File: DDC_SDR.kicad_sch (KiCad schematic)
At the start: 101 parts, among them J13 AWG_OUT, J14 DUT, J16 S21_OUT, J3 Filter, J4 Filter, J6 PMOD, Q10 2N7002, Q3 2N7002, U15 TPH2501-TR, U2 MS9280, U25 TPH2501-TR, U26 74LVC1G3157GW, U27 74LVC1G3157GW, U3 MS9708, U7 ICE40UP5K-SG48ITR

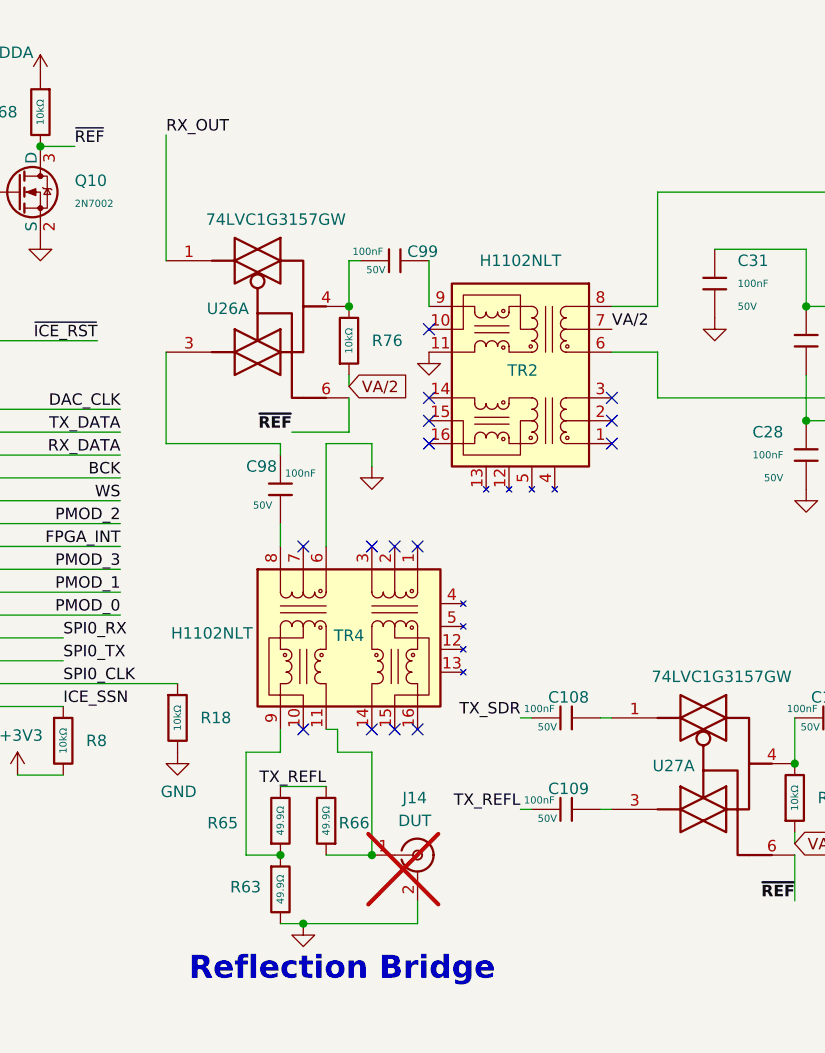
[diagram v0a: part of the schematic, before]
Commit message: Added provision for switch leakage current.
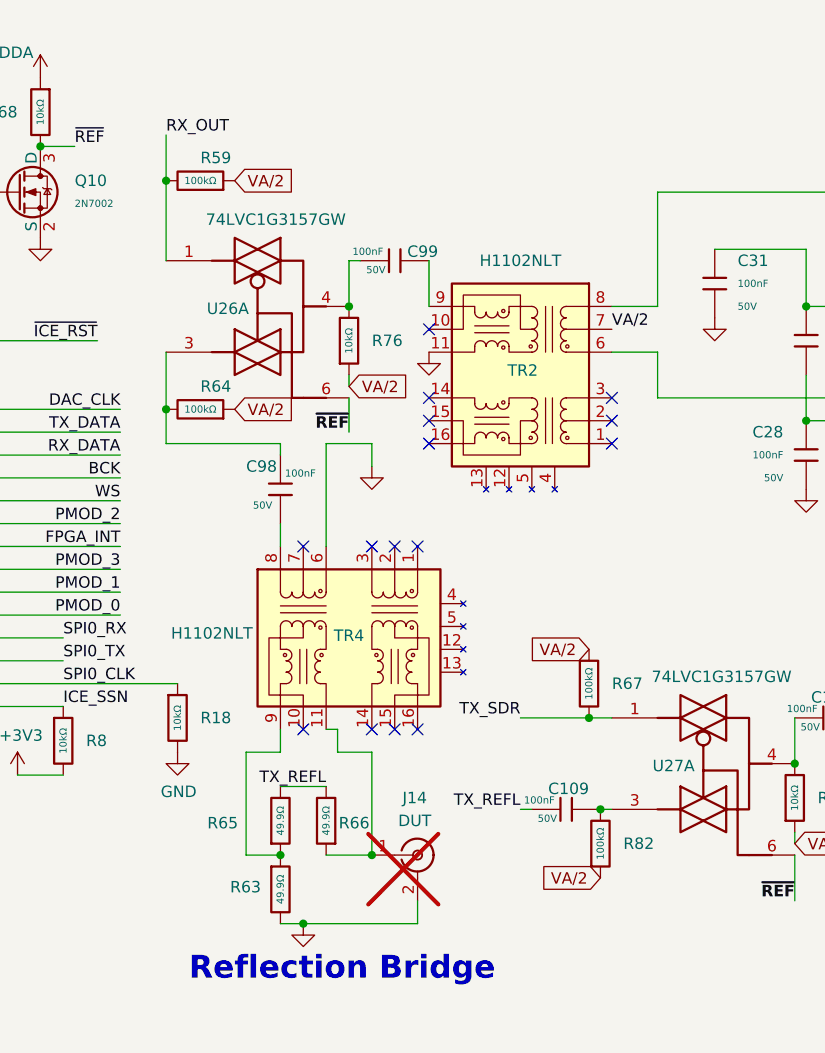
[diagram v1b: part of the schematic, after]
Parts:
- removed C108: 100nF, PCM_JLCPCB:C_0402, symbol PCM_JLCPCB-Capacitors:0402,100nF,(2)
- added R59, R64, R67, R82: 100kΩ, PCM_JLCPCB:R_0402, symbol PCM_JLCPCB-Resistors:0402,100kΩ
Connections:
- net RX_OUT: now also R59.2
- net TX_SDR: now also U27.1, R67.2
- net VA/2: now also R59.1, R64.1, R67.1, R82.1
- net at C98.1, U26.3: now also R64.2
- net at C109.2, U27.3: now also R82.2

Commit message: Minor tweaks...
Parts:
- added R83, R84: 22Ω, PCM_JLCPCB:R_0402, symbol PCM_JLCPCB-Resistors:0402,22Ω
- U7: Price $0.09 -> $8.49
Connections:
- net PMOD_3: now also JP51.2 (B), R30.2; no longer J6.4 (Pin_4), JP51.1 (A)
- net SPI0_RX: now also R83.1; no longer A2.6 (GPIO4)
- net SPI0_TX: now also R84.1; no longer A2.10 (GPIO7)
- new net: A2.10 (GPIO7), R84.2
- new net: A2.6 (GPIO4), R83.2
- new net: J6.4 (Pin_4), JP51.1 (A)
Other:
- note added: "Put the GBIN_PMOD_3 right by the PMOD connector. Then daisy-chain route this trace."
- note added: "WS (LRCK) pin must be BCK pin +1"
- note removed: "LRCK pin must be BCK pin +1"

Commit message: Starting to place components
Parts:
- A2: footprint Module:RaspberryPi_Pico_W_SMD_HandSolder -> Module:RaspberryPi_Pico_Common_THT
- C15: footprint PCM_JLCPCB:C_0805 -> PCM_JLCPCB:C_0603; symbol PCM_JLCPCB-Capacitors:0805,1uF -> PCM_JLCPCB-Capacitors:0603,1uF; LCSC C28323 -> C15849; Part CL21B105KBFNNNE -> CL10A105KB8NNNC; Price 0.012USD -> 0.008USD; Stock 4334256 -> 11535980; Temperature Coefficient X7R -> X5R
- C23, C30, C34, C93: footprint PCM_JLCPCB:C_0805 -> PCM_JLCPCB:C_0402; symbol PCM_JLCPCB-Capacitors:0805,100nF -> PCM_JLCPCB-Capacitors:0402,100nF,(2); LCSC C28233 -> C307331; Manufacturer (none) -> Samsung Electro-Mechanics; Part CL21B104KCFNNNE -> CL05B104KB54PNC; Price 0.009USD -> 0.008USD; Stock 1168020 -> 8389599; Voltage Rated 100V -> 50V
- C44: footprint PCM_JLCPCB:C_1206 -> PCM_JLCPCB:C_0805; symbol PCM_JLCPCB-Capacitors:1206,10uF -> PCM_JLCPCB-Capacitors:0805,10uF,(2); LCSC C13585 -> C440198; Manufacturer (none) -> Murata Electronics; Part CL31A106KBHNNNE -> GRM21BR61H106KE43L; Price 0.035USD -> 0.066USD; Stock 3698334 -> 1422246
- J3, J4: footprint (none) -> Connector_PinSocket_2.54mm:PinSocket_1x04_P2.54mm_Vertical
- J6: footprint (none) -> Connector_PinSocket_2.54mm:PinSocket_1x06_P2.54mm_Vertical
- R69: symbol PCM_JLCPCB-Resistors:0402,10kΩ -> PCM_JLCPCB-Resistors:0402,49.9Ω; LCSC C25744 -> C25120; Part 0402WGF1002TCE -> 0402WGF499JTCE; Resistance 10kΩ -> 49.9Ω; Stock 24372091 -> 464542
- U2, U3: footprint (none) -> Package_SO:TSSOP-28-1EP_4.4x9.7mm_P0.65mm_EP3.4x9.7mm_Mask3.1x4.05mm_ThermalVias
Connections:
- net D0: now also U7.34 (IOT_44b); no longer U7.23 (IOT_37a)
- net D1: now also U7.32 (IOT_43a); no longer U7.25 (IOT_36b)
- net D2: now also U7.28 (IOT_41a); no longer U7.26 (IOT_39a)
- net D3: now also U7.31 (IOT_42b); no longer U7.27 (IOT_38b)
- net D4: now also U7.27 (IOT_38b); no longer U7.28 (IOT_41a)
- net D5: now also U7.26 (IOT_39a); no longer U7.31 (IOT_42b)
- net D6: now also U7.25 (IOT_36b); no longer U7.32 (IOT_43a)
- net D7: now also U7.23 (IOT_37a); no longer U7.34 (IOT_44b)
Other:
- moved on the sheet: A2, C100, C101, C102, C103, C106, C107, C109, C15, C16, C18, C19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

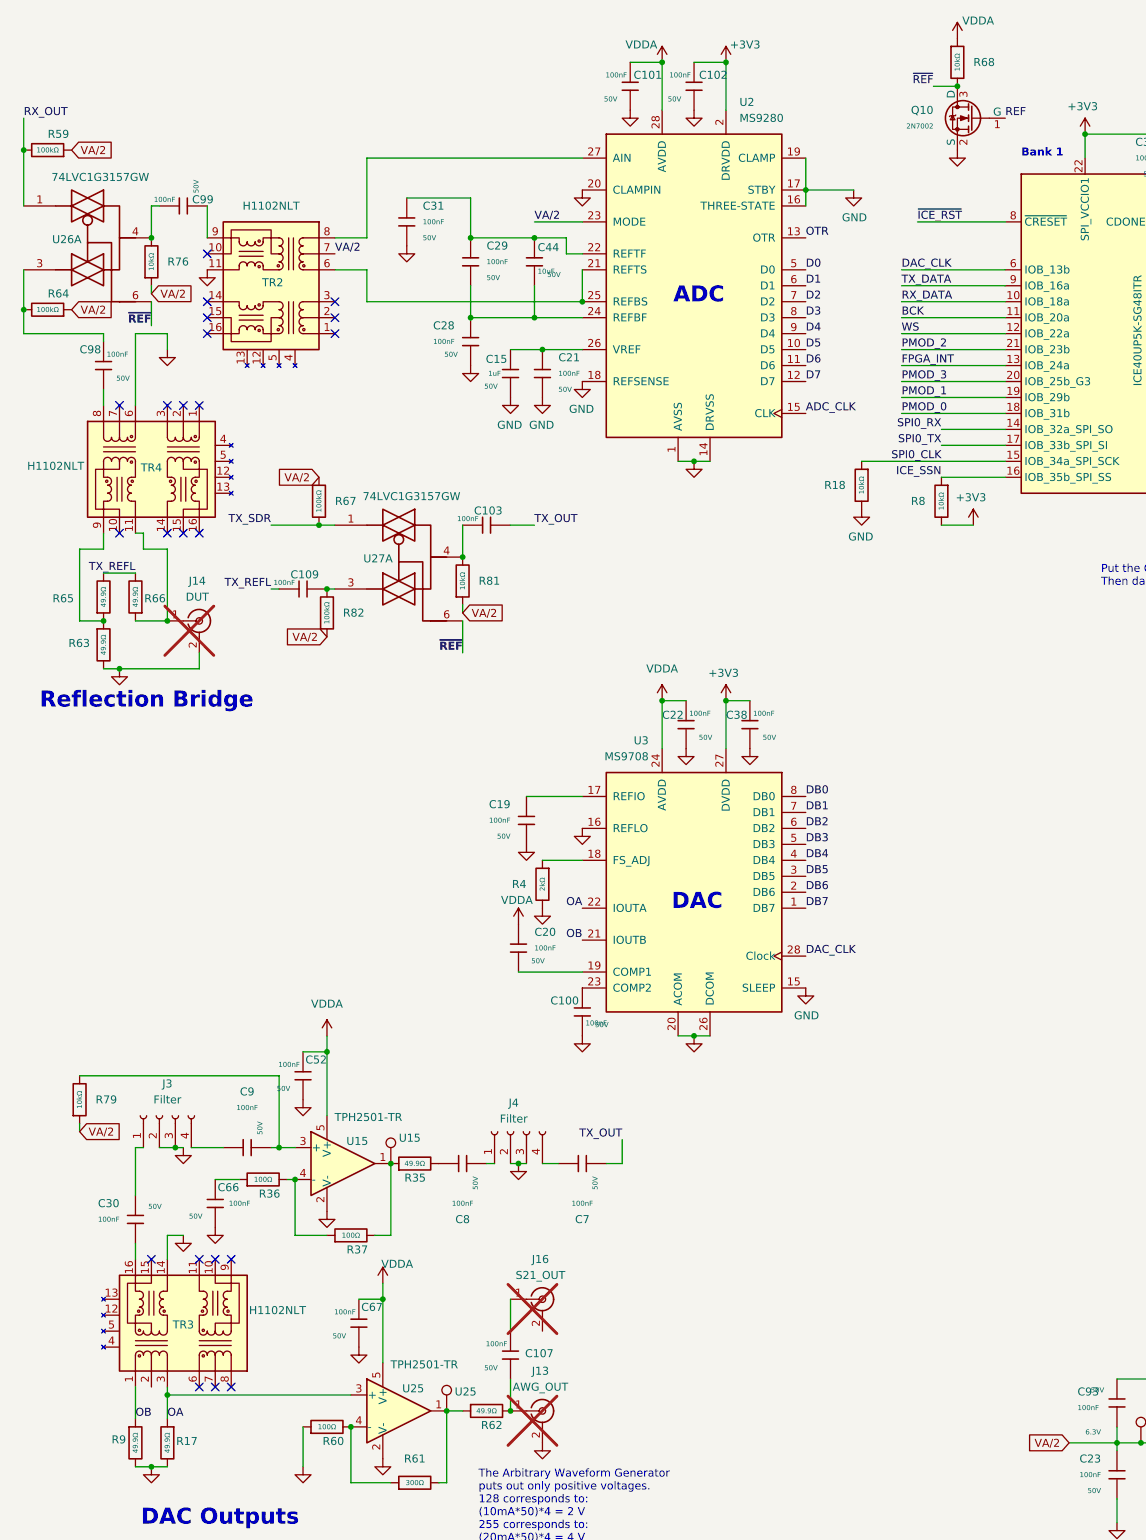
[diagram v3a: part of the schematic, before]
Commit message: Working on the analog chains
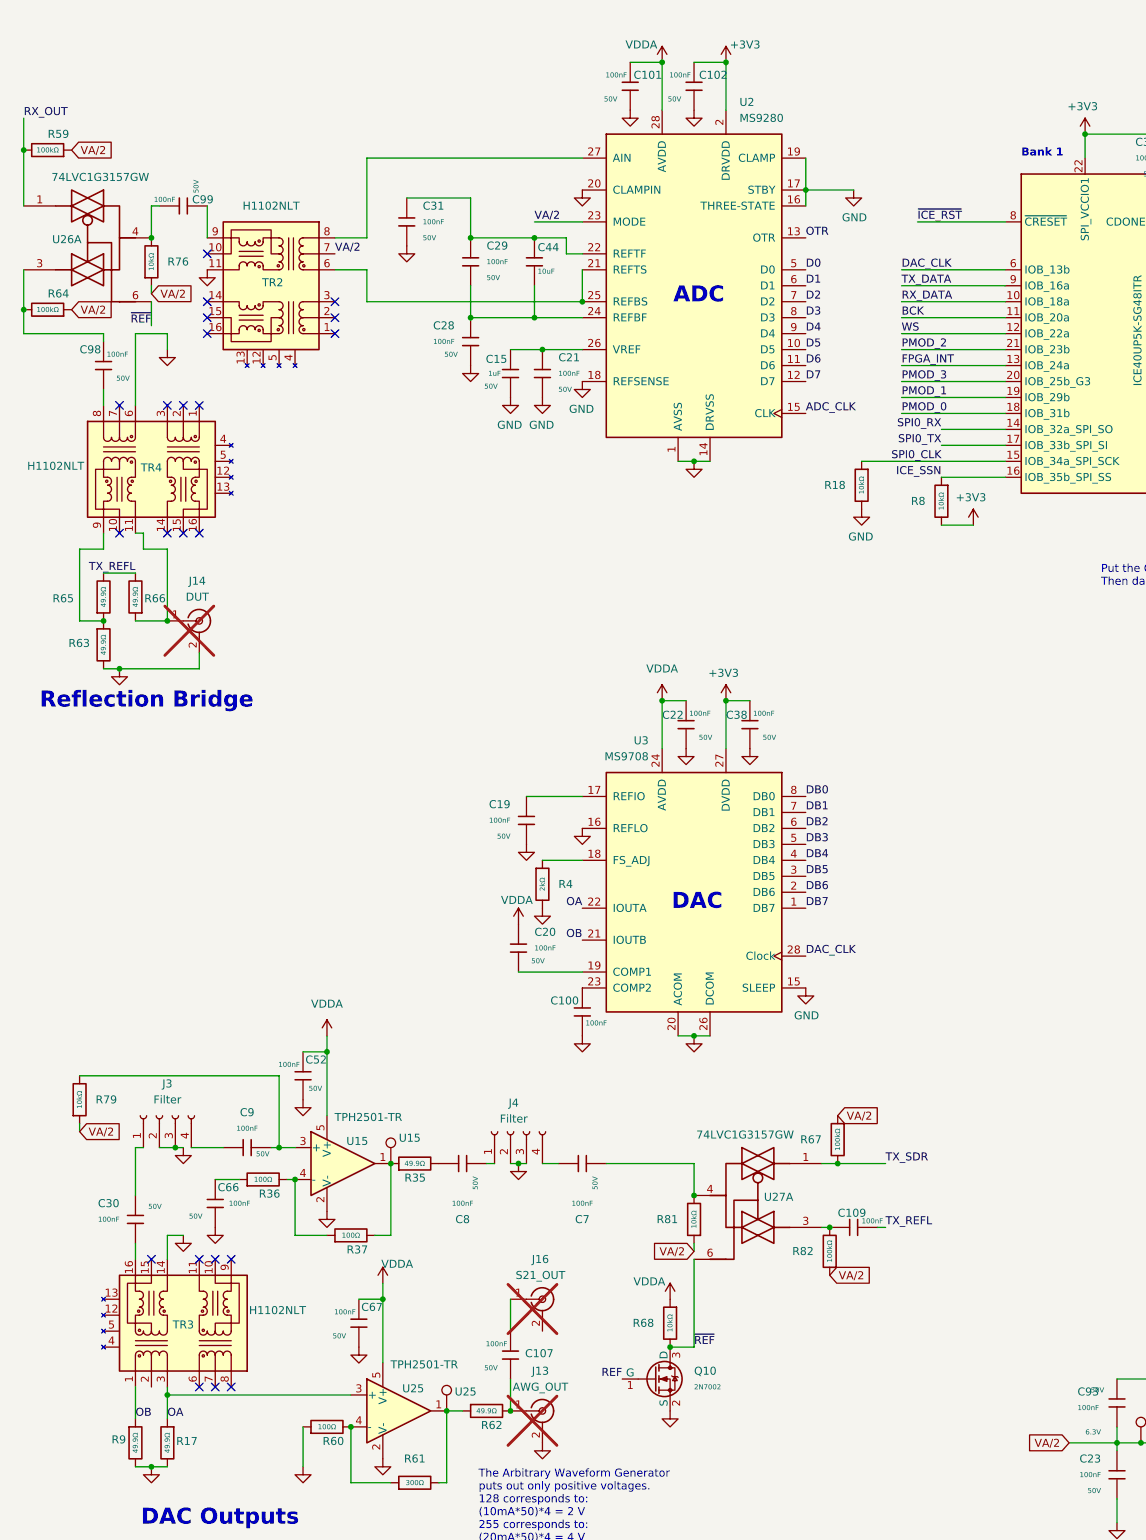
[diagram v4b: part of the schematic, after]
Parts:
- removed C103: 100nF, PCM_JLCPCB:C_0402, symbol PCM_JLCPCB-Capacitors:0402,100nF,(2)
- removed R4: 2kΩ, PCM_JLCPCB:R_0805, symbol PCM_JLCPCB-Resistors:0805,2kΩ
- added R4: 2kΩ, PCM_JLCPCB:R_0402, symbol PCM_JLCPCB-Resistors:0402,2kΩ
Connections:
- net TX_OUT is gone; now on an unnamed net: C7.2
- net GND: now also R4.2
- net at U3.18 (FS_ADJ): now also R4.1
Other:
- moved on the sheet: C109, Q10, R67, R68, R81, R82, U27A

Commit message: AF DAC Some VDDA Placed
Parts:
- removed R15, R16: 10kΩ, PCM_JLCPCB:R_0805, symbol PCM_JLCPCB-Resistors:0805,10kΩ
- added R23, R24: 10kΩ, PCM_JLCPCB:R_0402, symbol PCM_JLCPCB-Resistors:0402,10kΩ
- TR1: renamed from TR4; footprint Intro_to_CAD:XFMR_H1102NLT -> Transformer_SMD:Transformer_Ethernet_Wuerth_749013011A
- TR2: renamed from TR3; footprint Intro_to_CAD:XFMR_H1102NLT -> Transformer_SMD:Transformer_Ethernet_Wuerth_749013011A
- TR3: renamed from TR2; footprint Intro_to_CAD:XFMR_H1102NLT -> Transformer_SMD:Transformer_Ethernet_Wuerth_749013011A
- renumbered A2 to A1, C98 to C1, C29 to C10, C28 to C11, C15 to C12, C107 to C13, C20 to C14, C19 to C15, C44 to C16, C21 to C17, C100 to C18, C7 to C19, C30 to C2, C101 to C20, C22 to C21, C102 to C22, C38 to C23, C109 to C24, C93 to C25, C23 to C26, C32 to C27, C84 to C28, C91 to C29, C99 to C3, C63 to C30, C34 to C31, C18 to C32, C64 to C33, C97 to C34, C106 to C35, C16 to C36, C65 to C37, C66 to C4, C9 to C5, C52 to C6, C67 to C7, C31 to C8, C8 to C9, D7 to D1, D8 to D2, D6 to D3, J3 to J1, J14 to J2, J4 to J3, J16 to J4, J13 to J5, JP51 to JP1, JP4 to JP2, JP52 to JP3, JP50 to JP4, Q10 to Q1, Q3 to Q2, R59 to R1, R36 to R10, R60 to R11, R37 to R12, R35 to R13, R61 to R14, R62 to R15, R4 to R16, R68 to R17, R81 to R18, R82 to R19, R64 to R2, R67 to R20, R18 to R21, R8 to R22, R71 to R25, R70 to R26, R72 to R27, R69 to R28, R55 to R29, R79 to R3, R80 to R30, R14 to R31, R30 to R32, R83 to R33, R11 to R34, R84 to R35, R23 to R36, R13 to R37, R65 to R4, R63 to R5, R66 to R6, R9 to R7, R76 to R8, R17 to R9, TP29 to TP1, TP30 to TP2, TP13 to TP3, U26 to U1, U15 to U2, U25 to U3, U2 to U4, U3 to U5, U27 to U6
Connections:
- net GNDA: now also R24.2
- net VA/2: now also R23.2, R24.1
- net VDDA: now also R23.1

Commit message: SMA/LogicAnalyzer and VDDA placed
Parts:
- J2: value DUT -> S11; footprint Intro_to_CAD:Conn_Coaxial_Frohne -> Connector_Coaxial:SMA_Amphenol_132289_EdgeMount
- J4: footprint Intro_to_CAD:Conn_Coaxial_Frohne -> Connector_Coaxial:SMA_Amphenol_132289_EdgeMount
- J6: now fitted
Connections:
- net PMOD_0: now also U7.21 (IOB_23b); no longer U7.18 (IOB_31b)
- net PMOD_2: now also U7.18 (IOB_31b); no longer U7.21 (IOB_23b)
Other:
- note added: "PMOD connector will work as with an extra Pico as a logic analyzer using pins 29-24."
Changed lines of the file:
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@@
 		)
 	)
+	(text "PMOD connector will work\nas with an extra Pico as a\nlogic analyzer using pins\n29-24."
+		(exclude_from_sim no)
+		(at 204.47 78.994 0)
+		(effects
+			(font
+				(size 1.27 1.27)
+			)
+			(justify left)
+		)
+	)
 	(text "ADC"
 		(exclude_from_sim no)
@@
 	)
 	(label "PMOD_2"
-		(at 160.02 68.58 0)
+		(at 160.02 78.74 0)
 		(effects
 			(font
@@
 	)
 	(label "PMOD_0"
-		(at 160.02 78.74 0)
+		(at 160.02 68.58 0)
 		(effects
 			(font
@@
 		(on_board yes)
 		(in_pos_files yes)
-		(dnp yes)
+		(dnp no)
 		(fields_autoplaced yes)
 		(property "Reference" "J6"
@@
 			)
 		)
-		(property "Value" "DUT"
+		(property "Value" "S11"
 			(at 47.9426 107.95 0)
 			(show_name no)
@@
 			)
 		)
-		(property "Footprint" "Intro_to_CAD:Conn_Coaxial_Frohne"
+		(property "Footprint" "Connector_Coaxial:SMA_Amphenol_132289_EdgeMount"
 			(at 48.26 111.76 0)
 			(hide yes)
@@
 			)
 		)
-		(property "Description" ""
+		(property "Description" "SMA Connector"
 			(at 48.26 111.76 0)
 			(hide yes)
@@
 			)
 		)
-		(property "Footprint" "Intro_to_CAD:Conn_Coaxial_Frohne"
+		(property "Footprint" "Connector_Coaxial:SMA_Amphenol_132289_EdgeMount"
 			(at 102.87 219.71 0)
 			(hide yes)

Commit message: Fixed schematic errors, all placed
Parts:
- removed JP1: GBIN_PMOD_3, Jumper:SolderJumper-2_P1.3mm_Bridged2Bar_RoundedPad1.0x1.5mm, symbol Jumper:Jumper_2_Bridged
- Q1, Q2: symbol JLCPCB-Transistors:NMOS,2N7002 -> PCM_JLCPCB-Transistors:NMOS,2N7002K; Attrition Qty 5 -> 4; Category Transistors,MOSFETs -> Triode/MOS Tube/Transistor,MOSFETs; Class Basic Component -> Preferred Component; LCSC C8545 -> C22379475; Manufacturer Changjiang Electronics Tech (CJ) -> hongjiacheng; Part 2N7002 -> 2N7002K; Stock 1078050 -> 82639
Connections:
- net GNDA is gone; now on net GND: C26.1, C29.2, C31.1, R24.2
- net PMOD0 is gone; now on net PMOD_0: JP2.1 (A)
- net GND: now also J4.2 (Ext)
- net PMOD_3: now also J6.4 (Pin_4)
- no-connect marks 25 -> 26
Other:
- note added: "Then daisy-chain route PMOD_3 trace."
- note removed: "Put the GBIN_PMOD_3 right by the PMOD connector. Then daisy-chain route this trace."

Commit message: First wiring
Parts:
- U4: LCSC C1509022 -> C1509021
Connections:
- net D0: now also U7.25 (IOT_36b); no longer U7.34 (IOT_44b)
- net D1: now also U7.26 (IOT_39a); no longer U7.32 (IOT_43a)
- net D2: now also U7.27 (IOT_38b); no longer U7.28 (IOT_41a)
- net D3: now also U7.28 (IOT_41a); no longer U7.31 (IOT_42b)
- net D4: now also U7.31 (IOT_42b); no longer U7.27 (IOT_38b)
- net D5: now also U7.32 (IOT_43a); no longer U7.26 (IOT_39a)
- net D6: now also U7.34 (IOT_44b); no longer U7.25 (IOT_36b)
- net D7: now also U7.35 (IOT_46b_G0); no longer U7.23 (IOT_37a)
- net DB0: now also U7.4 (IOB_8a); no longer U7.44 (IOB_3b_G6)
- net DB1: now also U7.3 (IOB_9b); no longer U7.45 (IOB_5b)
- net DB2: now also U7.2 (IOB_6a); no longer U7.46 (IOB_0a)
- net DB3: now also U7.48 (IOB_4a); no longer U7.47 (IOB_2a)
- net DB4: now also U7.47 (IOB_2a); no longer U7.48 (IOB_4a)
- net DB5: now also U7.46 (IOB_0a); no longer U7.2 (IOB_6a)
- net DB6: now also U7.45 (IOB_5b); no longer U7.3 (IOB_9b)
- net DB7: now also U7.44 (IOB_3b_G6); no longer U7.4 (IOB_8a)
- net at R29.1: now also U7.23 (IOT_37a); no longer U7.35 (IOT_46b_G0)
- net A-: now reaches TR3.6 (RD+), U4.21 (REFTS), U4.25 (REFBS)
- net A+: now reaches TR3.8 (RD-), U4.27 (AIN)
- net OA renamed O+
- net OB renamed O-
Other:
- moved on the sheet: R29
